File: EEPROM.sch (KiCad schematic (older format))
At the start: 2 parts

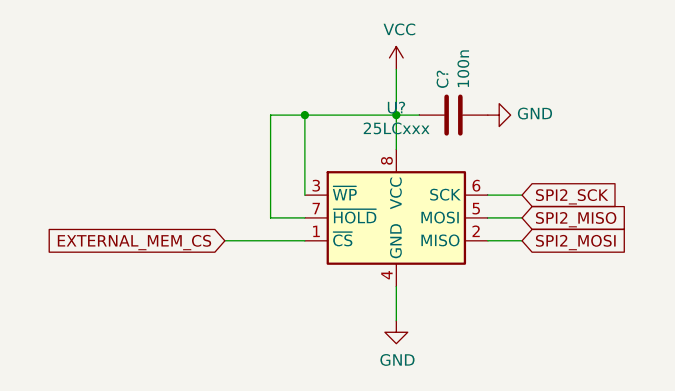
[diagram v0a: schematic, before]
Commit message: 4 layer add
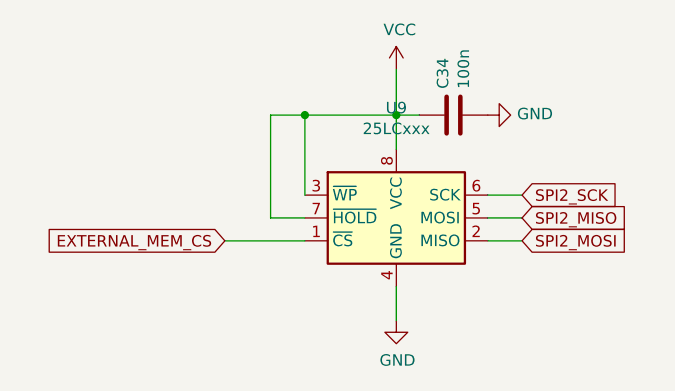
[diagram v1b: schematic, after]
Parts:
- gave numbers to parts that had none: 2
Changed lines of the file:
@@
 $Descr A4 11693 8268
 encoding utf-8
-Sheet 7 10
+Sheet 7 11
 Title ""
 Date ""
@@
 P 5250 3750
 AR Path="/5F6CB4BA" Ref="U?"  Part="1"
-AR Path="/5F5AF088/5F6CB4BA" Ref="U?"  Part="1"
-F 0 "U?" H 5250 4231 50  0000 C CNN
+AR Path="/5F5AF088/5F6CB4BA" Ref="U9"  Part="1"
+F 0 "U9" H 5250 4231 50  0000 C CNN
 F 1 "25LCxxx" H 5250 4140 50  0000 C CNN
 F 2 "" H 5250 3750 50  0001 C CNN
@@
 P 5250 3100
 AR Path="/5F6CB4C6" Ref="#PWR?"  Part="1"
-AR Path="/5F5AF088/5F6CB4C6" Ref="#PWR?"  Part="1"
-F 0 "#PWR?" H 5250 2950 50  0001 C CNN
+AR Path="/5F5AF088/5F6CB4C6" Ref="#PWR0144"  Part="1"
+F 0 "#PWR0144" H 5250 2950 50  0001 C CNN
 F 1 "VCC" H 5265 3273 50  0000 C CNN
 F 2 "" H 5250 3100 50  0001 C CNN
@@
 P 5250 4200
 AR Path="/5F6CB4D5" Ref="#PWR?"  Part="1"
-AR Path="/5F5AF088/5F6CB4D5" Ref="#PWR?"  Part="1"
-F 0 "#PWR?" H 5250 3950 50  0001 C CNN
+AR Path="/5F5AF088/5F6CB4D5" Ref="#PWR0145"  Part="1"
+F 0 "#PWR0145" H 5250 3950 50  0001 C CNN
 F 1 "GND" H 5255 4027 50  0000 C CNN
 F 2 "" H 5250 4200 50  0001 C CNN
@@
 AR Path="/5F53A524/5F6CC7D6" Ref="C?"  Part="1"
 AR Path="/5F5517E4/5F6CC7D6" Ref="C?"  Part="1"
-F 0 "C?" H 5615 3346 50  0000 L CNN
+AR Path="/5F5AF088/5F6CC7D6" Ref="C34"  Part="1"
+F 0 "C34" H 5615 3346 50  0000 L CNN
 F 1 "100n" H 5615 3255 50  0000 L CNN
 F 2 "Capacitor_SMD:C_0603_1608Metric" H 5538 3150 50  0001 C CNN
@@
 	5350 3300 5250 3300
 $Comp
-L power:GND #PWR?
+L power:GND #PWR0146
 U 1 1 5F6CD00A
 P 5650 3300
-F 0 "#PWR?" H 5650 3050 50  0001 C CNN
+F 0 "#PWR0146" H 5650 3050 50  0001 C CNN
 F 1 "GND" V 5655 3172 50  0000 R CNN
 F 2 "" H 5650 3300 50  0001 C CNN

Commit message: a
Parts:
- U9: footprint (none) -> Package_SO:SOIC-8-1EP_3.9x4.9mm_P1.27mm_EP2.29x3mm
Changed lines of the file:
@@
 $Descr A4 11693 8268
 encoding utf-8
-Sheet 7 11
+Sheet 6 11
 Title ""
 Date ""
@@
 F 0 "U9" H 5250 4231 50  0000 C CNN
 F 1 "25LCxxx" H 5250 4140 50  0000 C CNN
-F 2 "" H 5250 3750 50  0001 C CNN
+F 2 "Package_SO:SOIC-8-1EP_3.9x4.9mm_P1.27mm_EP2.29x3mm" H 5250 3750 50  0001 C CNN
 F 3 "http://ww1.microchip.com/downloads/en/DeviceDoc/21832H.pdf" H 5250 3750 50  0001 C CNN
 	1    5250 3750
